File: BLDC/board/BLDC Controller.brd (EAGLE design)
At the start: 100 x 70.3 mm, 113 parts, among them IC1 DRV8301, IC2 OPA2374, IC3 Encoder, IC4 INA199A1, IC5 TPS51103, M1 FRDM-KL05Z, M2 MBED_NXP_LPC1768, Q1 MOSFET-NCHANNELSMD, Q2 MOSFET-NCHANNELSMD, Q3 P-CHANNEL-MOSFETTO252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

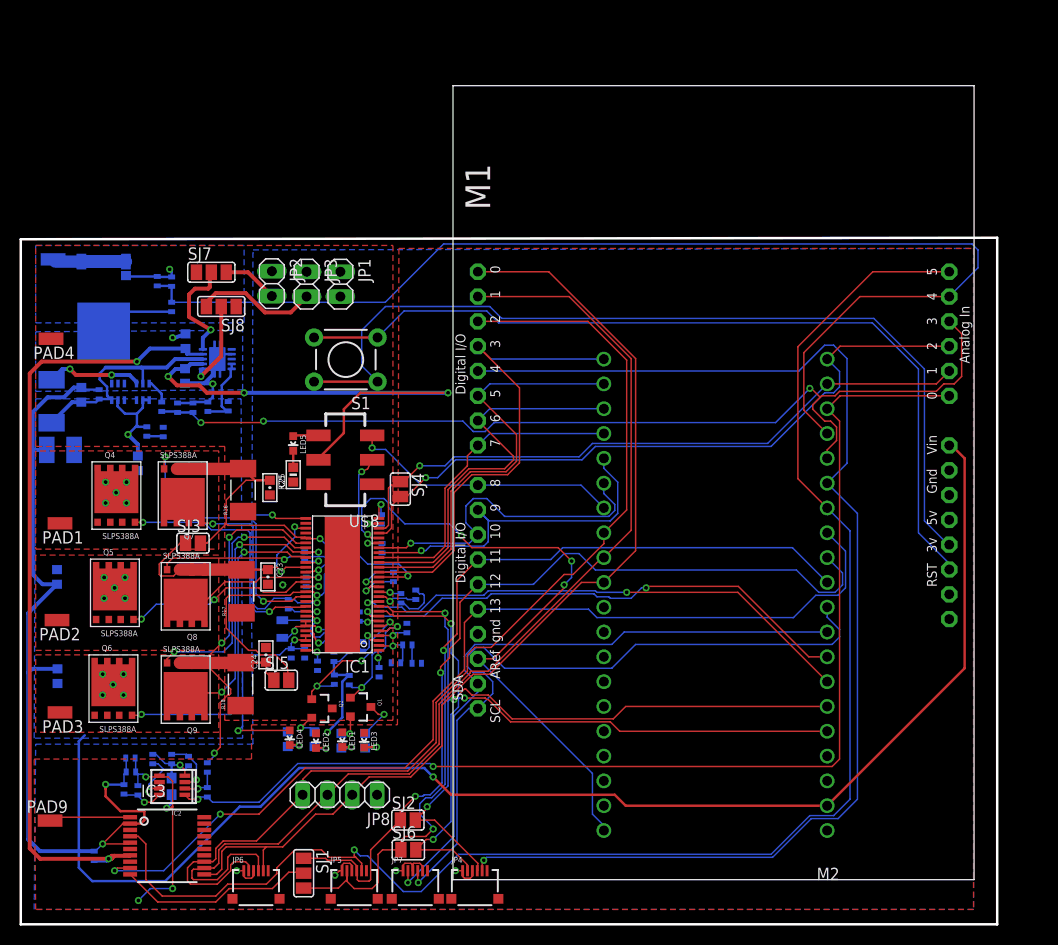
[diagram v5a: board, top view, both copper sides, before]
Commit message: Fixed DRC to have 6mil clearance, fixed DRC errors.
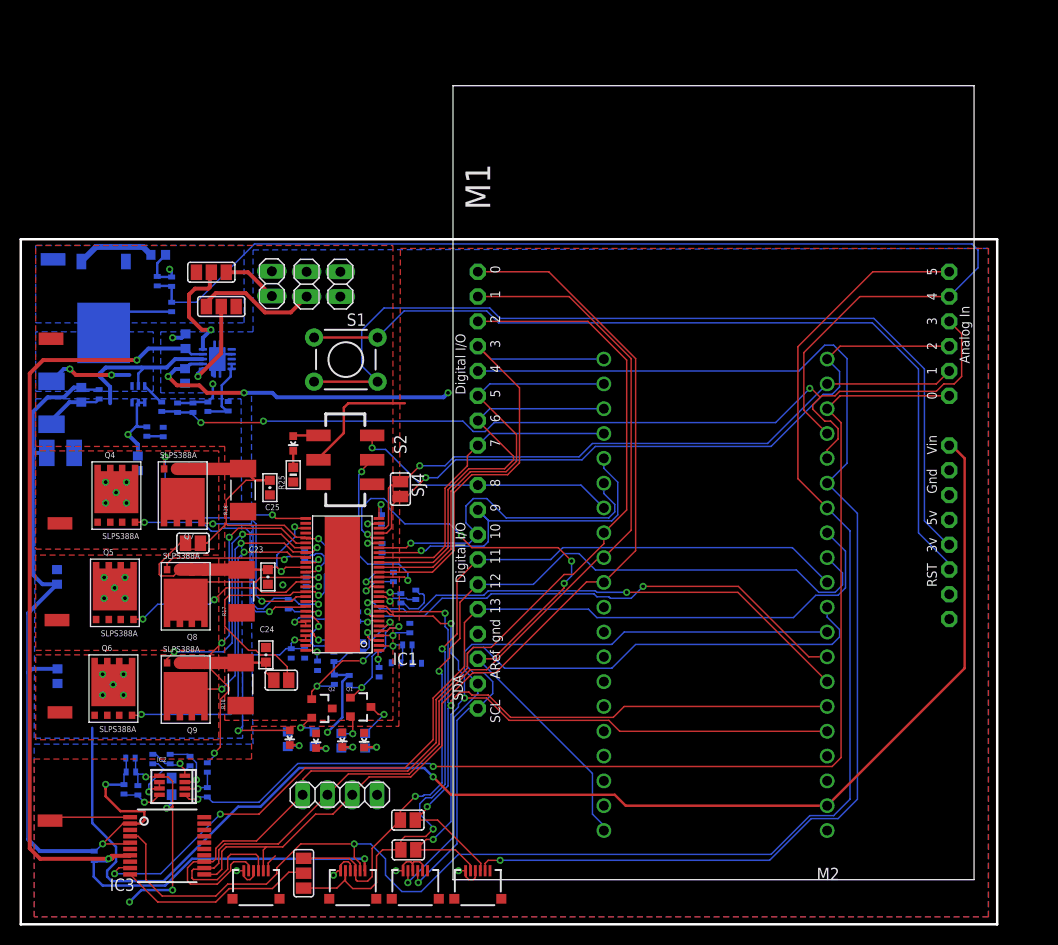
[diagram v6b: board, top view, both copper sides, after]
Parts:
- removed IC4, U$4: INA199A1, modular_robotics:SC70-6
- added ICN: INA199A1, modular_robotics:SC70-6
- IC3: value Encoder -> AS 5134
- JP4: value MOLEX_503480-0600 -> 4x MOLEX_503480-0600
- moved L1 6.22 mm to (33.0, 30.6), turned to 270 degrees
- moved R13 3.58 mm to (14.1, 68.4), turned to 0 degrees
- moved C18 0.30 mm to (4.06, 48.1)
- moved JP4 0.30 mm to (46.8, 3.61)
- moved R5 0.30 mm to (39.8, 30.2)
- moved JP5 0.15 mm to (34.0, 3.61)
- moved R21 0.15 mm to (17.3, 16.6)
- moved R30 0.15 mm to (3.15, 53.2)
- moved R6 0.15 mm to (34.5, 31.3)
- moved R24 0.15 mm to (15.3, 16.8)
- renumbered U$8 to S2
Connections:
- removed net V+: IC4.3
- net 3.3V: no longer JP5.6
- net 5V: now also JP5.6
- net GND: now also ICN.1, ICN.2; no longer IC4.1, IC4.2, U$4.2
- net I_BATT: now also ICN.4; no longer IC4.4
- net N$18: now also ICN.6; no longer IC4.6
- net V_BATT: now also ICN.3, ICN.5; no longer IC4.5, U$4.3
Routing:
- net 5V: track 81.1 -> 113.0 mm, vias 2 -> 3
- net GND: track 157.1 -> 149.1 mm
- net BAT+: track 7.56 -> 0.00 mm
- net 3.3V: track 101.3 -> 97.6 mm
- net SH_B: track 16.3 -> 19.7 mm
- net N$9: track 4.68 -> 8.08 mm
- net ENC_CS: track 156.5 -> 158.1 mm
- net I_BATT: track 17.7 -> 16.6 mm
- net V_BATT: track 220.6 -> 219.8 mm
- net VSENSE: track 5.31 -> 5.92 mm
- net AVDD: track 3.16 -> 2.61 mm
- net PH: track 11.2 -> 11.7 mm, vias 2 -> 1
- net EN_GATE: track 19.5 -> 20.0 mm
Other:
- board size 100 x 70.3 mm -> 100 x 70.1 mm
- board text added: "3.3V"
- board text added: "Douglas Hutchings Biomimetic Milisystems Labaratory 2014.9.28 Brushless DC Motor Controller Rev. A"
- board text added: "FAULT"
- board text added: "G D_MOSI G D_MISO EXT_CS 3.3"
- board text added: "G E_MOSI G E_MISO E_CS 5"
- board text added: "G SDA G SCL G 3.3"
- board text added: "G W G V U 3.3"
- board text added: "MOTOR_ENABLED"
- board text added: "OCTW"
- board text added: "SPI Drv & Enc Tie-in"
- board text added: "V_BATT"
- board text added: "W V U GND"

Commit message: Added bigger GND planes, motor mount holes
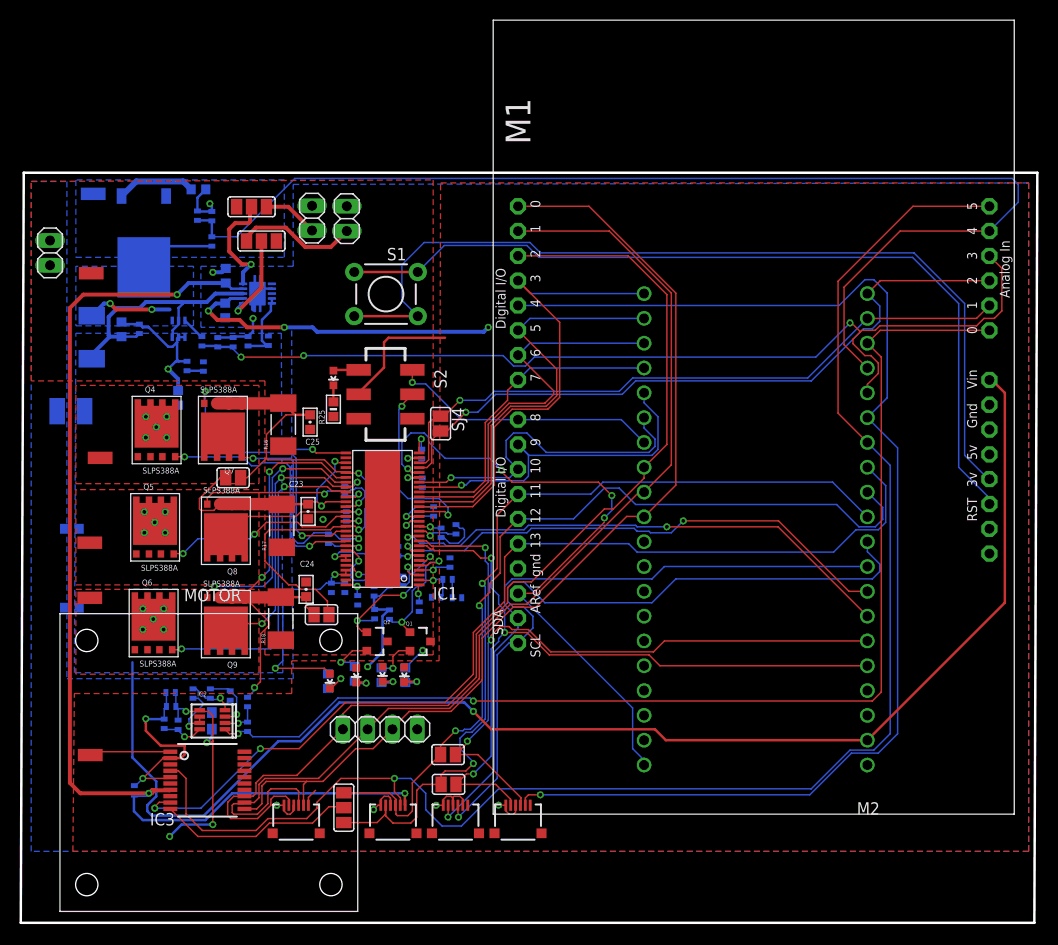
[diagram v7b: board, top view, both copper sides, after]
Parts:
- added MOTOR: (no value), biomimetic:S-1804MOTOR
- moved JP1 29.9 mm to (3.00, 68.6)
- moved PAD3 12.1 mm to (7.06, 33.3)
- moved Q1 9.06 mm to (40.8, 28.8)
- moved Q2 8.88 mm to (36.4, 28.8)
- moved PAD2 8.60 mm to (7.06, 38.9)
- moved C17 7.87 mm to (16.1, 53.7)
- moved C29 7.87 mm to (18.1, 72.4)
- moved C3 7.87 mm to (43.0, 39.9)
- moved C5 7.87 mm to (41.1, 45.1)
- moved C7 7.87 mm to (34.5, 33.0)
- moved C8 7.87 mm to (33.3, 41.6)
- moved PAD5 7.87 mm to (7.42, 74.6)
- moved Q3 7.87 mm to (12.6, 69.6)
- moved Q7 7.87 mm to (18.4, 47.3)
- moved R12 7.87 mm to (18.7, 56.9)
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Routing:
- net GND: track 149.1 -> 87.3 mm
- net V_BATT: track 219.8 -> 224.9 mm
- net N$6: track 3.16 -> 4.74 mm
- net N$5: track 3.08 -> 4.38 mm
- net N$10: track 2.20 -> 3.27 mm
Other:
- board size 100 x 70.1 mm -> 104.1 x 76.8 mm
